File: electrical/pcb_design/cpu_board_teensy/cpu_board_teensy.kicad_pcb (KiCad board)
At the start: 2 copper layers, 82.5 x 82.5 mm, 9 parts, among them J1 Molex_504050-1291, U1 Teensy4.0_TopPinsOnly, U2 RFM69HCW, U3 BNO085_Adafruit_Breakout_I2C, U4 BMP390_Adafruit_Breakout

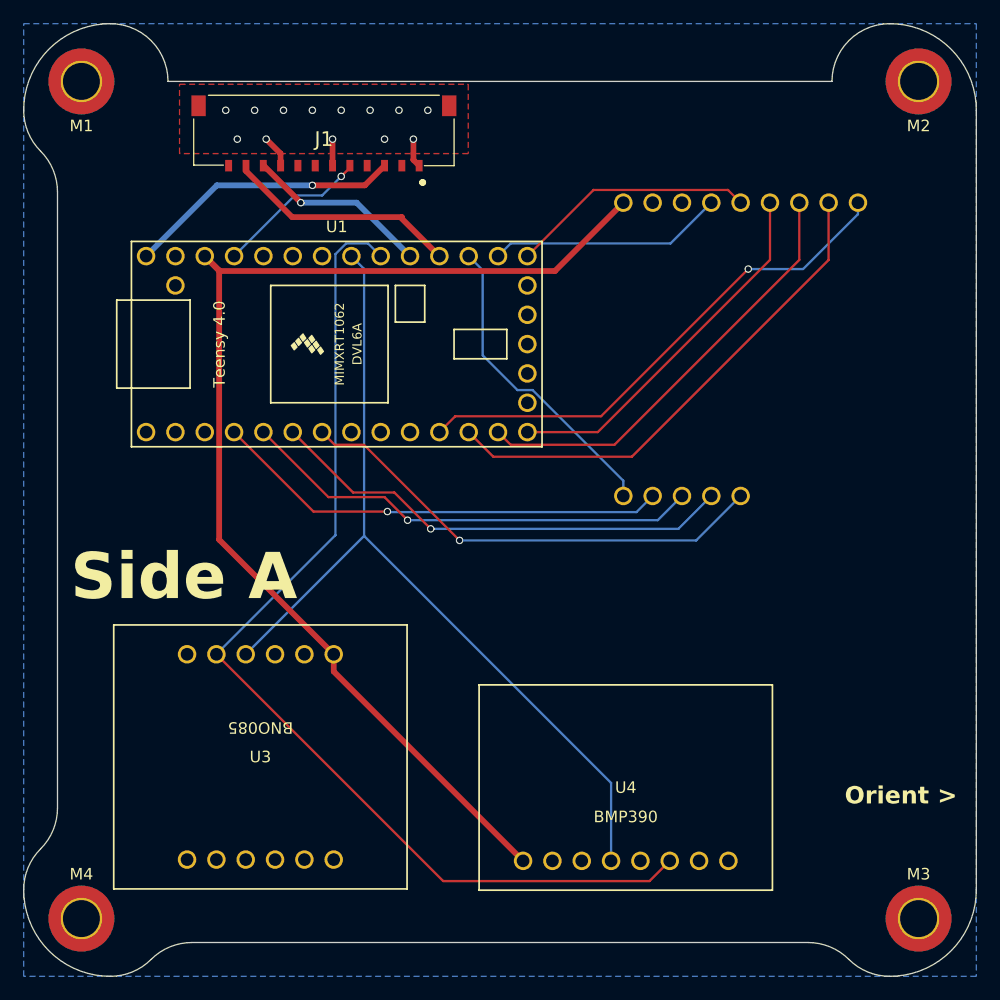
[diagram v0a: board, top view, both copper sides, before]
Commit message: Adding support for PWM signals to magnetorquers and heating shroud. Still missing footprints and proper symbols for these headers. Also, signal routing has been temporarily removed until these parts can be placed.
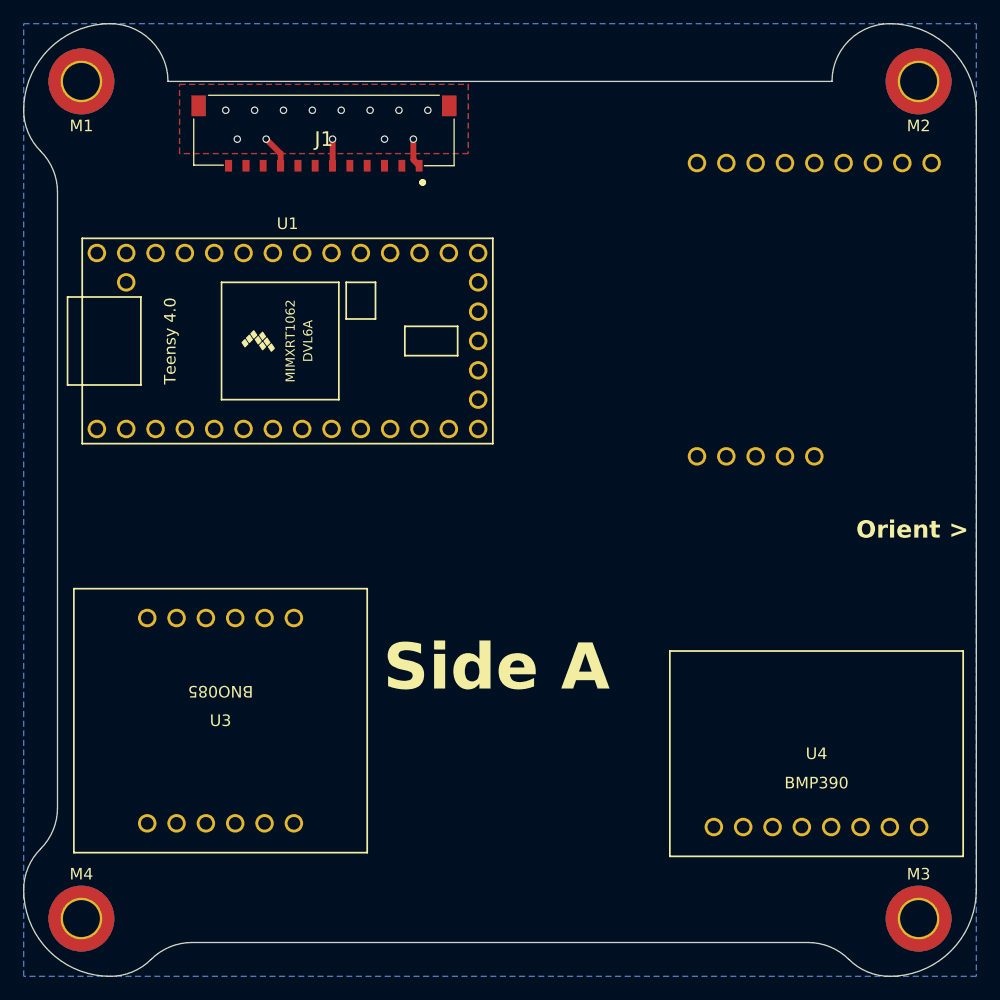
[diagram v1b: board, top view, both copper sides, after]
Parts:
- M1, M2, M3, M4: value ~ -> M3
- moved U4 16.8 mm to (168.7, 130.7)
- moved U2 7.24 mm to (168.5, 92.3)
- moved U3 4.66 mm to (117.0, 127.9)
- moved U1 4.27 mm to (122.8, 95.0)
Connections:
- U1 pad 10: unconnected-(U1-8_TX2_IN1-Pad10) -> /MAG_PWM_4
- U1 pad 2: unconnected-(U1-0_RX1_CRX2_CS1-Pad2) -> /MAG_PWM_0
- U1 pad 27: unconnected-(U1-20_A6_TX5_LRCLK1-Pad27) -> CHARGER_INT
- U1 pad 29: unconnected-(U1-22_A8_CTX1-Pad29) -> /MAG_PWM_5
- U1 pad 3: unconnected-(U1-1_TX1_CTX2_MISO1-Pad3) -> /MAG_PWM_1
- U1 pad 30: CHARGER_INT -> /HEATER_PWM
- U1 pad 8: unconnected-(U1-6_OUT1D-Pad8) -> /MAG_PWM_2
- U1 pad 9: unconnected-(U1-7_RX2_OUT1A-Pad9) -> /MAG_PWM_3
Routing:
- net +3V3: track 103.0 -> 0.00 mm
- net LOCAL_SDA: track 91.8 -> 0.00 mm
- net LOCAL_SCL: track 76.2 -> 0.00 mm
- net /RADIO_RESET: track 45.2 -> 0.00 mm, vias 1 -> 0
- net /CS: track 44.1 -> 0.00 mm
- net /GPIO_5: track 41.7 -> 0.00 mm, vias 1 -> 0
- net /GPIO_4: track 40.9 -> 0.00 mm, vias 1 -> 0
- net /GPIO_3: track 40.3 -> 0.00 mm, vias 1 -> 0
- net /GPIO_2: track 39.7 -> 0.00 mm, vias 1 -> 0
- net /MOSI: track 38.1 -> 0.00 mm
- net /MISO: track 32.1 -> 0.00 mm
- net /GPIO_1: track 27.1 -> 0.00 mm
- net +5V: track 23.9 -> 0.00 mm, vias 1 -> 0
- net /SCK: track 21.3 -> 0.00 mm
- net /GPIO_0: track 20.4 -> 0.00 mm
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
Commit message: Finished iteration on Teensy CPU board
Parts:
- added J2: HEATER_PWM, footprints:Molex_5013310607, F.Cu at (142.5, 78.5)
- added J3: MAGNETORQUER_PWM_0, footprints:Molex_5013310607, F.Cu at (150.8, 78.5)
- added J4: MAGNETORQUER_PWM_1, footprints:Molex_5013310607, F.Cu at (176.5, 113.5)
- added J5: MAGNETORQUER_PWM_2, footprints:Molex_5013310607, F.Cu at (151.4, 141.0)
- added J6: MAGNETORQUER_PWM_3, footprints:Molex_5013310607, F.Cu at (143.4, 141.0)
- added J7: MAGNETORQUER_PWM_4, footprints:Molex_5013310607, F.Cu at (135.4, 141.0)
- added J8: MAGNETORQUER_PWM_5, footprints:Molex_5013310607, F.Cu at (108.8, 110.5)
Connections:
- J1 pad 2: unconnected-(J1-Pad2) -> VCC
- J1 pad 4: unconnected-(J1-Pad4) -> +3.3VA
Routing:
- net +3.3VA: track 0.00 -> 197.6 mm, vias 0 -> 8
- net +5V: track 0.00 -> 182.5 mm, vias 0 -> 8
- net VCC: track 0.00 -> 176.3 mm, vias 0 -> 8
- net +3V3: track 0.00 -> 139.4 mm, vias 0 -> 1
- net LOCAL_SDA: track 0.00 -> 120.7 mm, vias 0 -> 2
- net LOCAL_SCL: track 0.00 -> 111.2 mm, vias 0 -> 2
- net /MAG_PWM_1: track 0.00 -> 75.3 mm
- net /RADIO_RESET: track 0.00 -> 61.0 mm
- net GND: track 7.62 -> 66.6 mm, vias 13 -> 32
- net /GPIO_3: track 0.00 -> 58.4 mm, vias 0 -> 2
- net /GPIO_4: track 0.00 -> 58.0 mm, vias 0 -> 2
- net /MAG_PWM_2: track 0.00 -> 57.7 mm
- net /GPIO_2: track 0.00 -> 57.2 mm, vias 0 -> 2
- net /CS: track 0.00 -> 56.1 mm
- net /MAG_PWM_0: track 0.00 -> 55.6 mm
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
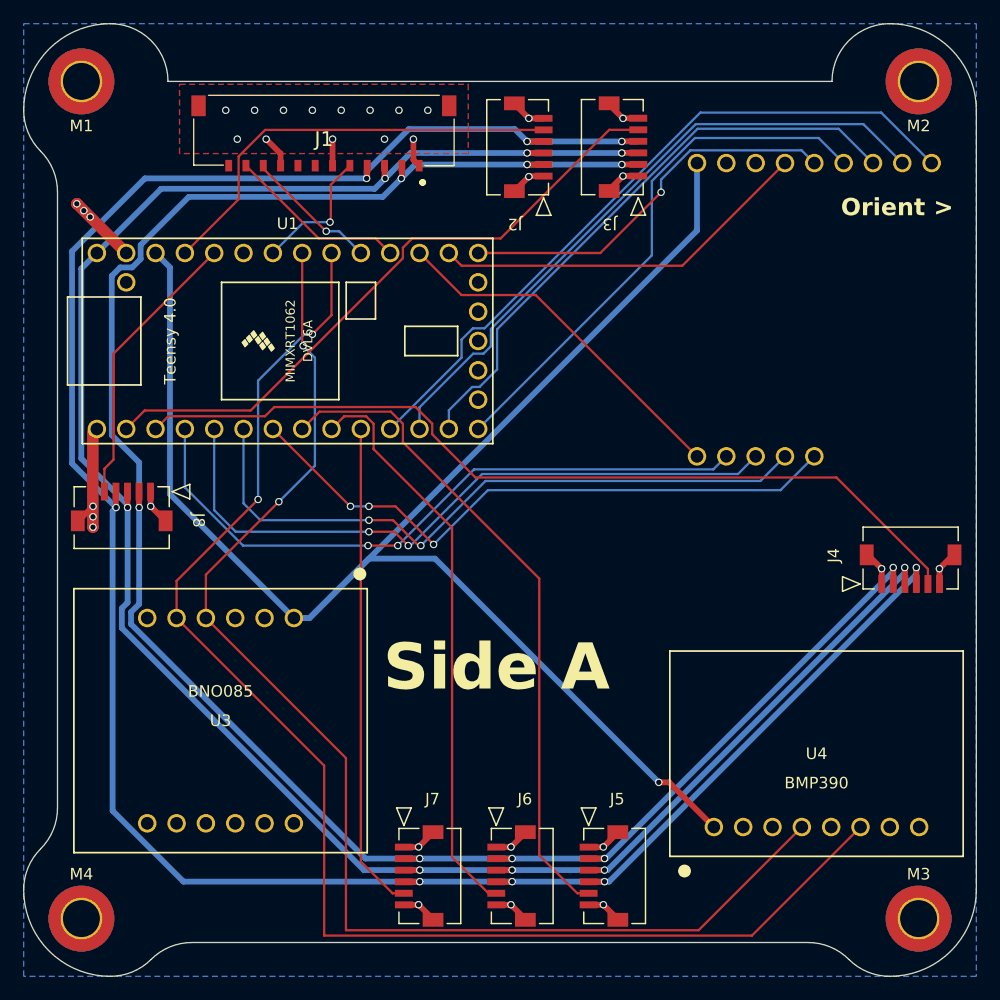
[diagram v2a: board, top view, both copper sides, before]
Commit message: Attempted to fix footprint origin of Molex 5013310607. Not successful, but found workaround when ordering from JLCPCB.
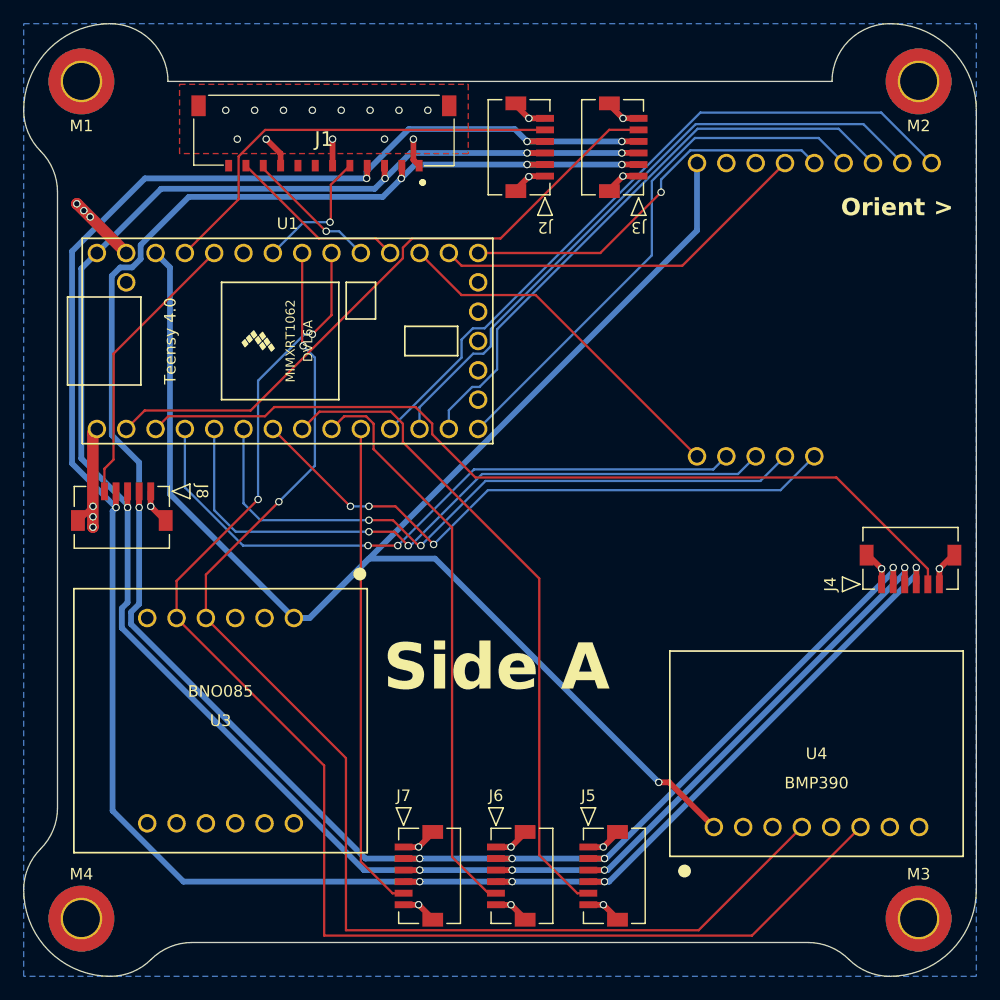
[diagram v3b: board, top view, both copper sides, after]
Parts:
- U4: value BMP390_Adafruit_Breakout -> BMP390
- moved J2 6.23 mm to (146.7, 83.2), turned to -90 degrees
- moved J3 6.17 mm to (154.8, 83.2), turned to -90 degrees
- moved J8 6.17 mm to (113.5, 106.5), turned to 0 degrees
- moved J4 6.17 mm to (171.8, 117.5), turned to 180 degrees
- moved J5 6.17 mm to (147.4, 136.3), turned to 90 degrees
- moved J6 6.17 mm to (139.4, 136.3), turned to 90 degrees
- moved J7 6.17 mm to (131.4, 136.3), turned to 90 degrees

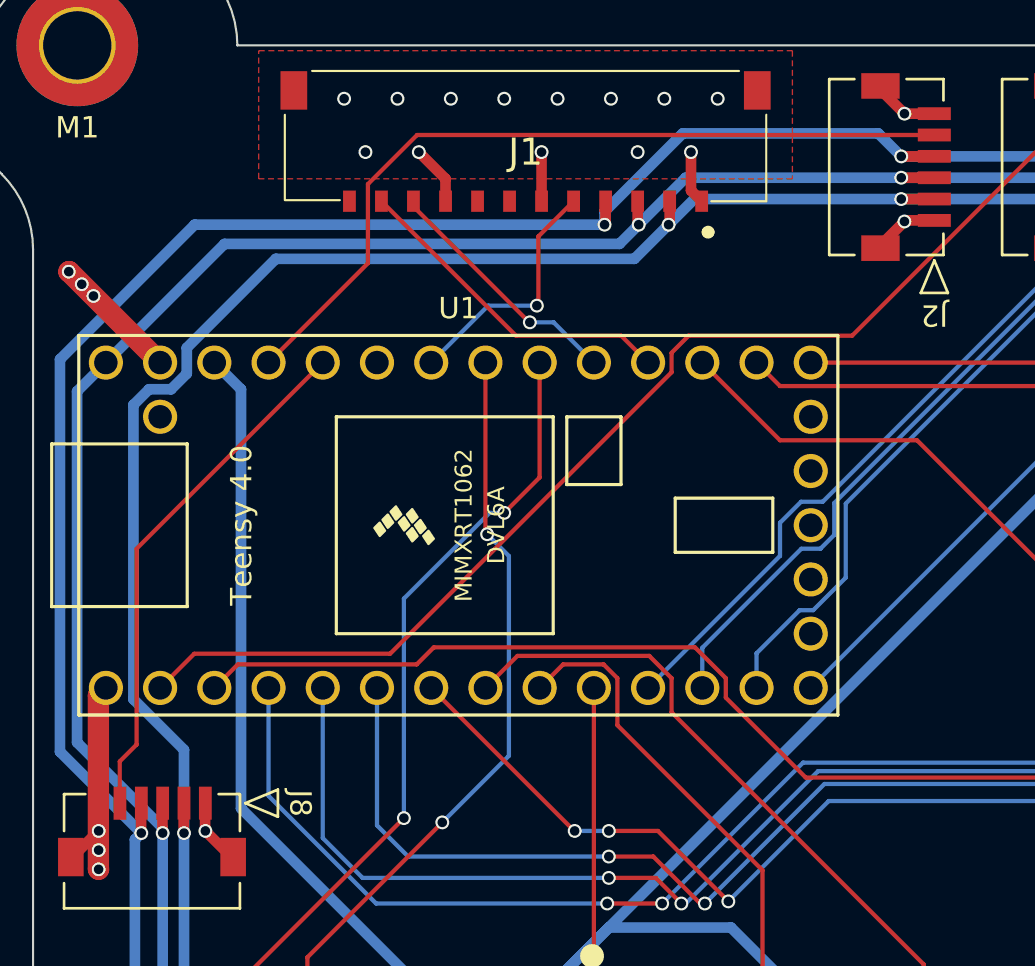
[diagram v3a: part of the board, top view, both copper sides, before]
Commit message: Fixed major bug where header orientations need to be swapped on different ends of the cabling.
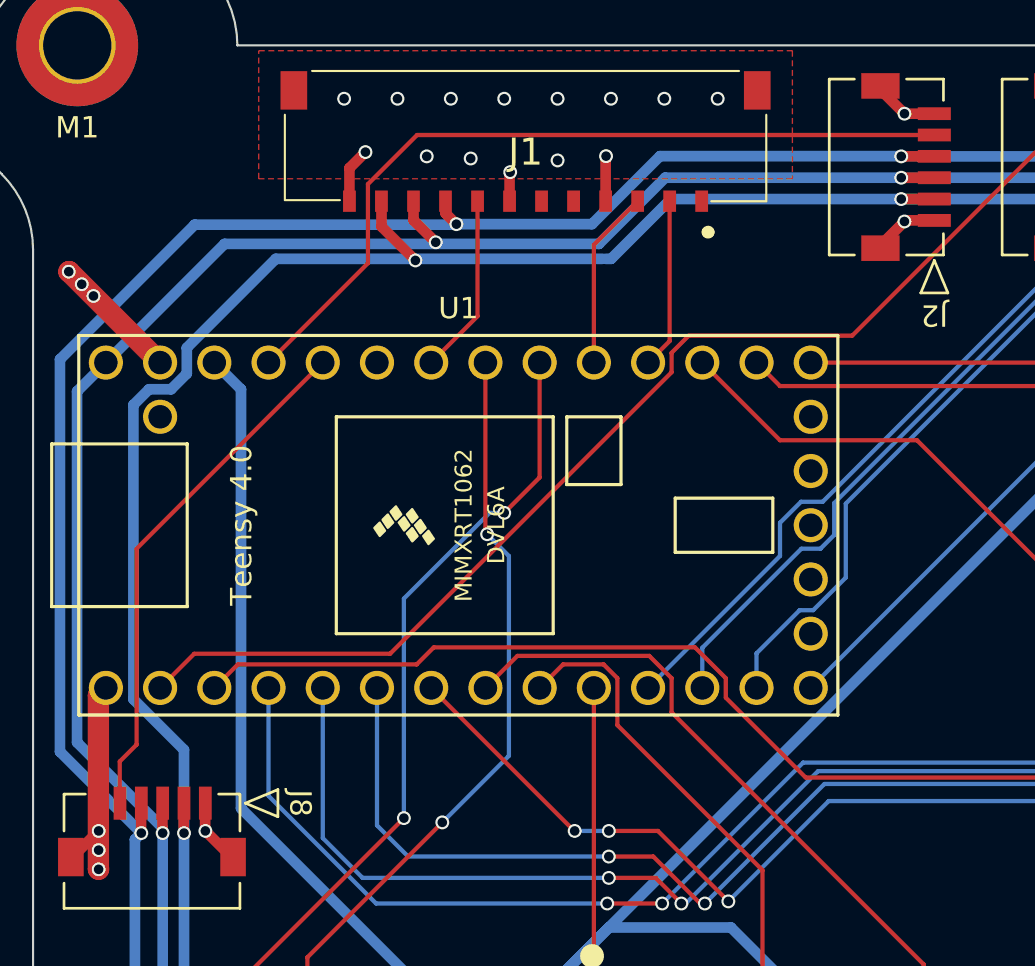
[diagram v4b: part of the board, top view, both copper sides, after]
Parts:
- J1: value Molex_504050-1291 -> Interconnect_Power_CPU-Power_side
- U4: value BMP390 -> BMP390_Adafruit_Breakout
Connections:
- J1 pad 1: GND -> unconnected-(J1-+3V3-Pad1)
- J1 pad 10: REMOTE_SDA -> +5V
- J1 pad 11: REMOTE_SCL -> VCC
- J1 pad 12: unconnected-(J1-Pad12) -> GND
- J1 pad 2: VCC -> REMOTE_SCL
- J1 pad 3: +5V -> REMOTE_SDA
- J1 pad 4: +3.3VA -> GND
- J1 pad 5: CHARGER_INT -> unconnected-(J1-UNUSED-Pad5)
- J1 pad 6: GND -> unconnected-(J1-UNUSED-Pad6)
- J1 pad 7: unconnected-(J1-Pad7) -> GND
- J1 pad 8: unconnected-(J1-Pad8) -> CHARGER_INT
- J1 pad 9: GND -> +3.3VA
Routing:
- net REMOTE_SCL: track 15.6 -> 7.98 mm
- net REMOTE_SDA: track 11.7 -> 8.41 mm, vias 1 -> 0
- net CHARGER_INT: track 11.7 -> 8.46 mm, vias 1 -> 0
- net VCC: track 176.3 -> 178.4 mm
- net GND: track 66.6 -> 65.1 mm, vias 32 -> 33
- net +5V: track 182.5 -> 184.0 mm
- net +3.3VA: track 197.6 -> 196.6 mm
